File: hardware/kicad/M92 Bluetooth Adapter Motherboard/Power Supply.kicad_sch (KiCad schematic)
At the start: 35 parts, among them IC11 MCP1702T-5002E_CB, IC12 TPS22810DBVR, IC13 TPS22917DBVR, IC4 NJU7031D, IC4 TL7660IDR, J1 Conn_External_Power, J4 B2B-XH-A, J5 B2B-XH-A, J9 B6B-XH-A

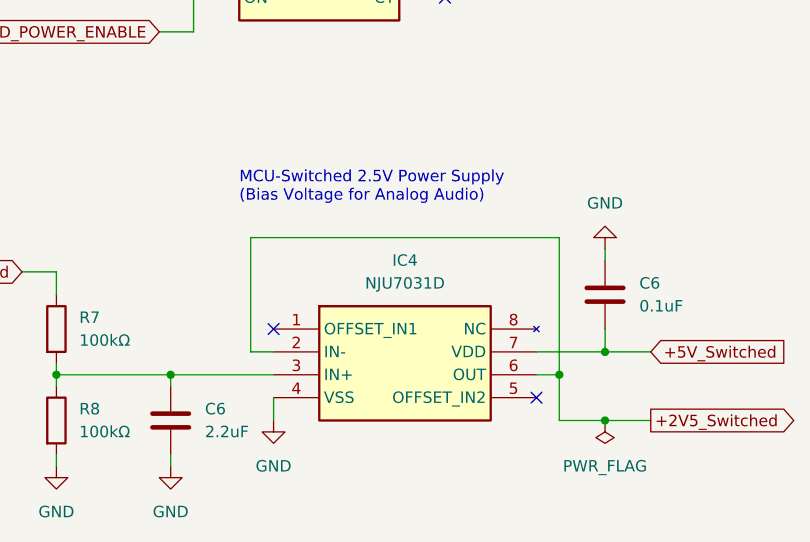
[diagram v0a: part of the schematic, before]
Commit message: Rework load switch enable circuitry/code
Rework load switch enable circuitry/code to fix brief power-on glitch when initially connecting battery power.
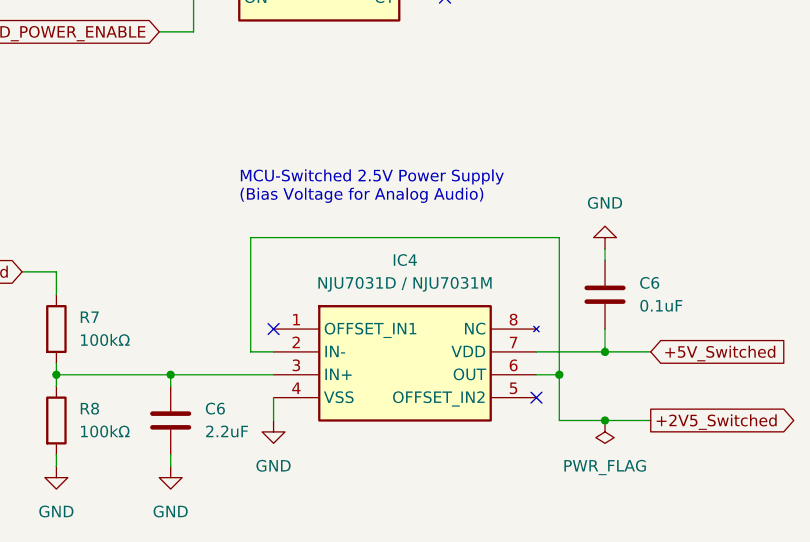
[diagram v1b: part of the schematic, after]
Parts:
- IC4: value NJU7031D -> NJU7031D / NJU7031M
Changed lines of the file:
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@@
       (effects (font (size 1.27 1.27)))
     )
-    (property "Value" "NJU7031D" (at 88.265 168.91 0)
+    (property "Value" "NJU7031D / NJU7031M" (at 88.265 168.91 0)
       (effects (font (size 1.27 1.27)))
     )

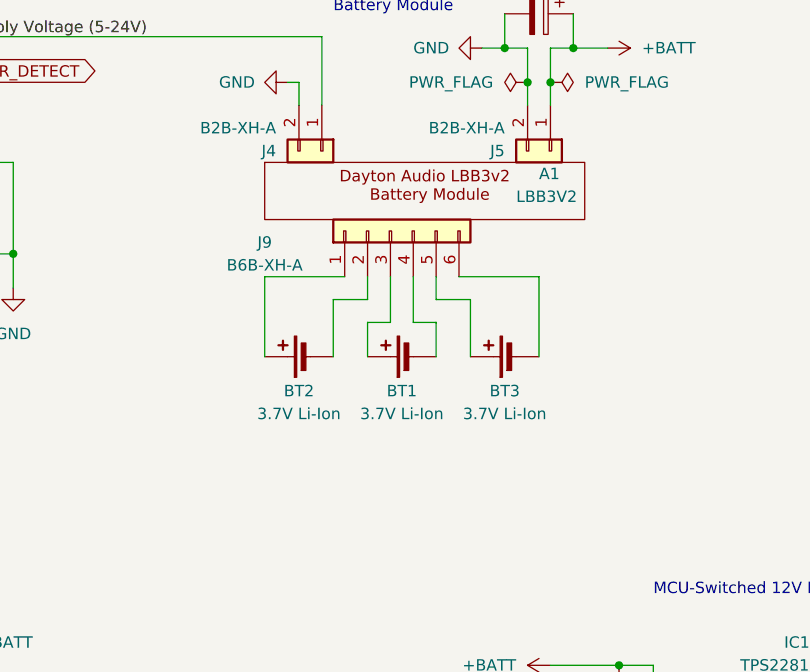
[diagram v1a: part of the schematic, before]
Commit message: Partial motherboard PCB updates for test fitting
This is a partial update to the motherboard PCB layout just so I can get some prototype boards manufactured and test fit with some updated/relocated components before committing to laying out the new custom battery/power management circuitry.

* Removed representation of Dayton Audio battery module PCB (will be replaced by custom battery circuitry in future).
* Relocated battery holders, and updated their footprints for sturdier part.
* Added pin headers for mounting the new programming port PCB.
* Adjusted positions of several mounting holes in attempt to match reality better (based on actual fitment of the PCB).
* Adjusted position of BT module connector slightly right in attempt to match reality better (based on actual fitment of the PCB).
* Adjusted footprint of mic jack to use oval PTH.
* Adjusted mic jack position further toward front edge of board to protrude more like original car phone mic jack.
* Added custom 3D models for BT module connector, RJ45 socket, and coax antenna port.
* Added coax antenna port and programming port to the PCB layout for spatial reference (not on schematic)
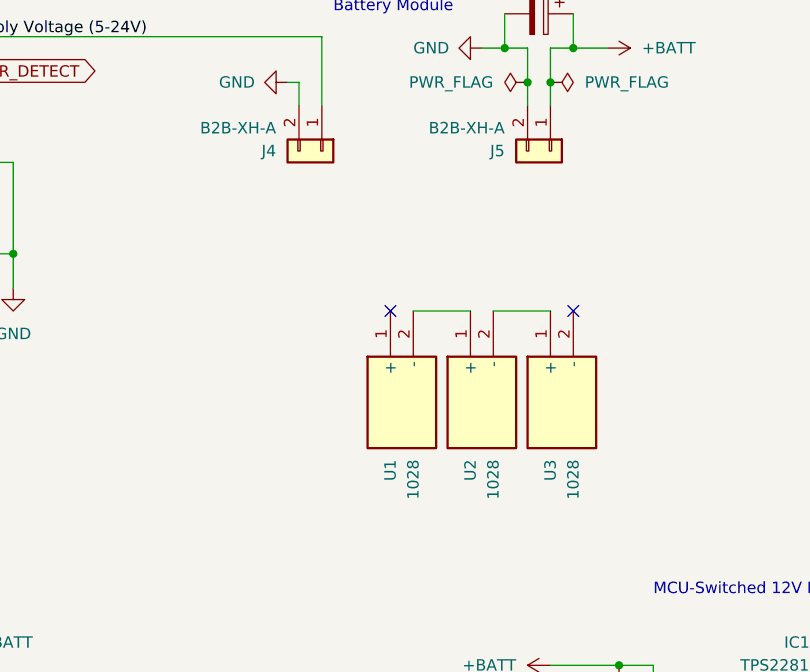
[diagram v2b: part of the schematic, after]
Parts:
- removed A1: LBB3V2, M92 Bluetooth Adapter Motherboard:LBB3v2 Battery Module, symbol M92 Bluetooth Adapter Motherboard:LBB3V2
- removed BT1, BT2, BT3: 3.7V Li-Ion, Battery:BatteryHolder_Keystone_2460_1xAA, symbol Device:Battery_Cell
- removed J9: B6B-XH-A, Connector_JST:JST_XH_B6B-XH-A_1x06_P2.50mm_Vertical, symbol Connector_Generic:Conn_01x06
- added U1, U2, U3: 1028, SamacSys_Parts:1028, symbol SamacSys_Parts:1028
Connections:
- new net: U1.2 (-), U2.1 (+)
- new net: U2.2 (-), U3.1 (+)
- no-connect marks 6 -> 8

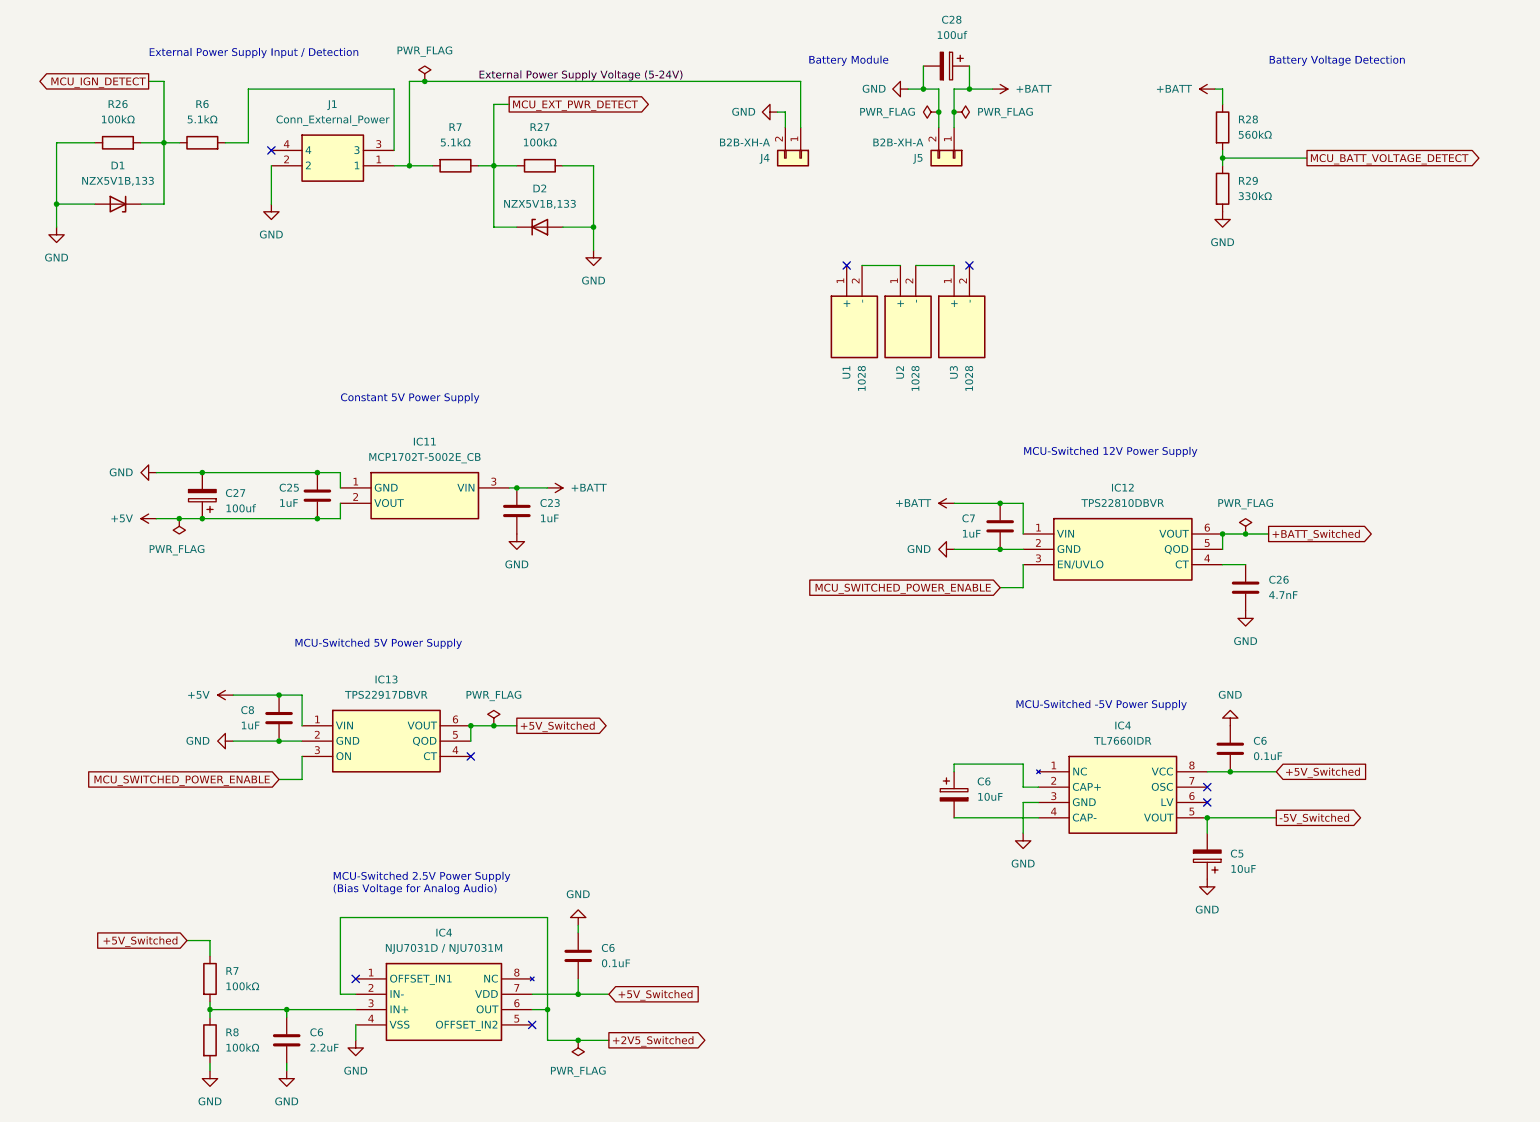
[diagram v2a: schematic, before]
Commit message: Add new battery module to motherboard schematic
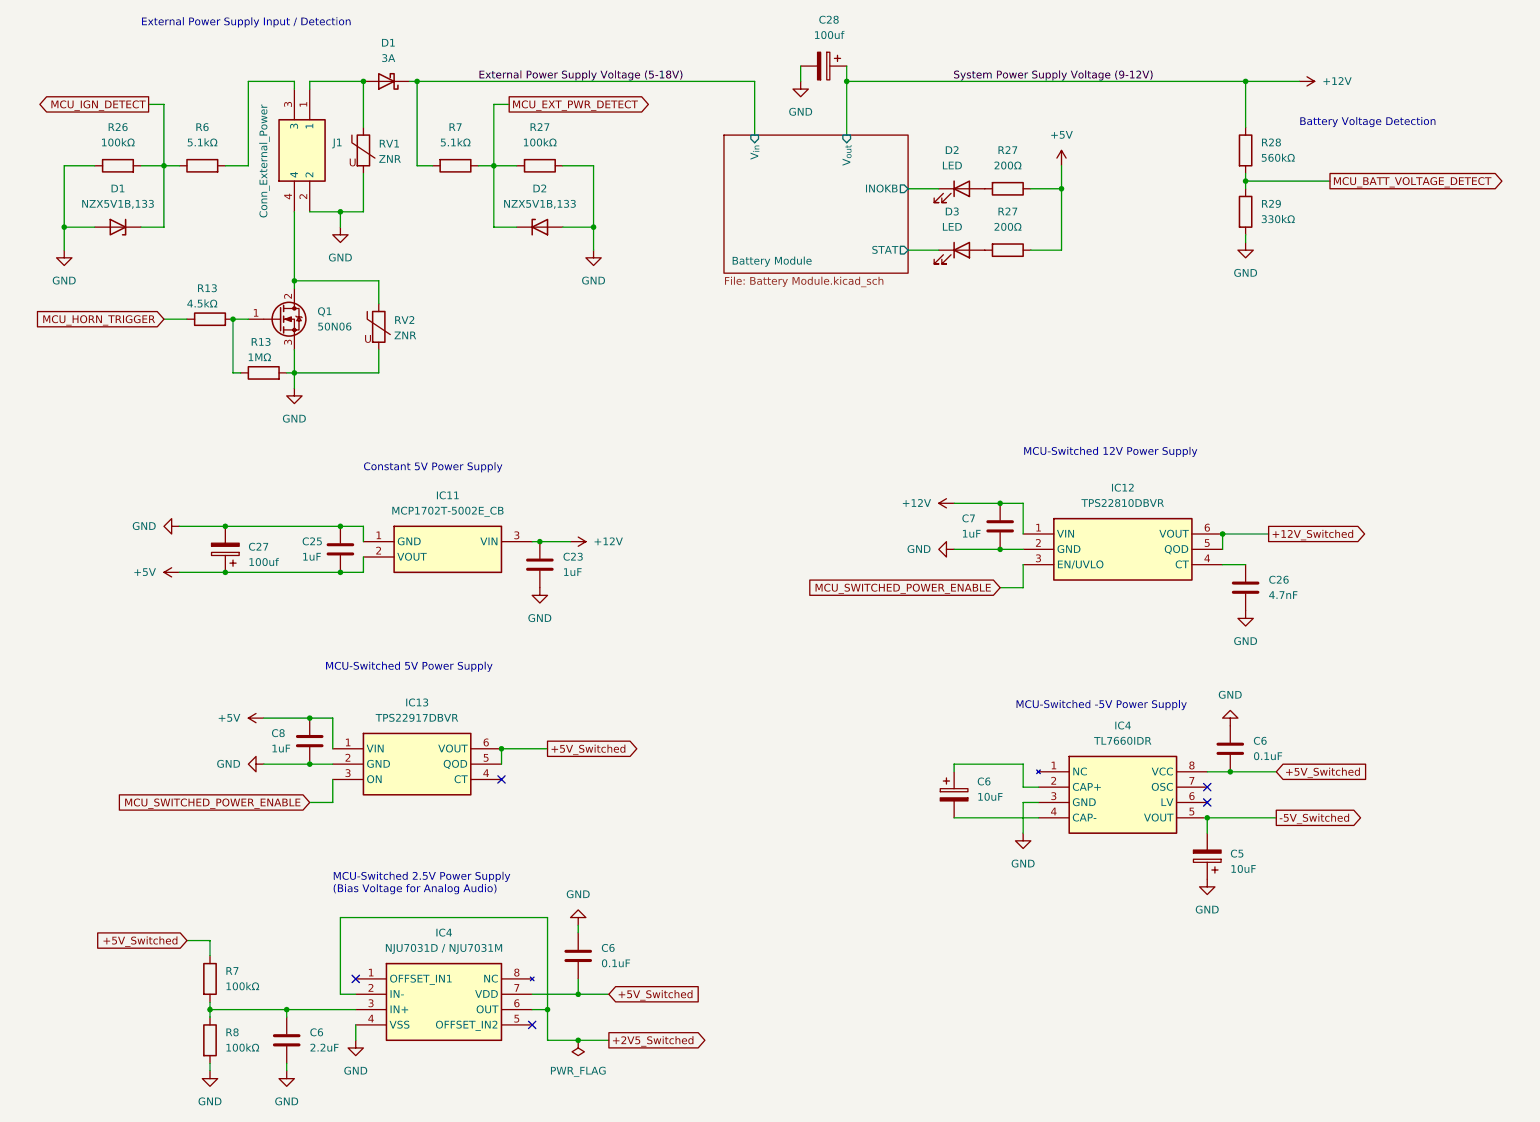
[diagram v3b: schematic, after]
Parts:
- removed J4, J5: B2B-XH-A, Connector_JST:JST_XH_B2B-XH-A_1x02_P2.50mm_Vertical, symbol Connector_Generic:Conn_01x02
- removed U1, U2, U3: 1028, SamacSys_Parts:1028, symbol SamacSys_Parts:1028
- added D1: 3A, Diode_THT:D_DO-201AD_P12.70mm_Horizontal, symbol Device:D_Schottky
- added D2, D3: LED, LED_SMD:LED_0805_2012Metric, symbol Device:LED
- added Q1: 50N06, Package_TO_SOT_SMD:TO-252-2, symbol Device:Q_NMOS_GDS
- added R13: 4.5kΩ, Resistor_SMD:R_0402_1005Metric, symbol Device:R
- added R13: 1MΩ, Resistor_SMD:R_0402_1005Metric, symbol Device:R
- added R27 (x2): 200Ω, Resistor_SMD:R_0402_1005Metric, symbol Device:R
- added RV1, RV2: ZNR, M92 Bluetooth Adapter Motherboard:ERZV10D270, symbol Device:Varistor
- IC11: Mouser Price/Stock https://www.mouser.com/ProductDetail/Microchip-Technology/M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 -> https://www.mouser.co.uk/ProductDetail/Microchip-Technology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
- IC12, IC13: Mouser Price/Stock https://www.mouser.com/ProductDetail/Texas-Instruments/TPS2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 -> https://www.mouser.co.uk/ProductDetail/Texas-Instruments/TP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
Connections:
- net +5V: now also R27.1, R27.1
- net GND: now also Q1.3 (S), R13.2, RV1.2, RV2.2
- net at J1.4: now also Q1.2 (D), RV2.1
- net +BATT renamed +12V
- net +BATT_Switched renamed +12V_Switched
- net External Power Supply Voltage (5-24V): no longer names the net of J1.1
- net External Power Supply Voltage (5-24V): now also D1.2 (A), RV1.1; no longer R7.2
- new net: D3.2 (A), R27.2
- new net: Q1.1 (G), R13.1, R13.2
- new net: D2.2 (A), R27.2
- new net Battery Module/INOKB: D2.1 (K)
- new net Battery Module/STAT: D3.1 (K)
- new net External Power Supply Voltage (5-18V): D1.1 (K), R7.2
- new net MCU_HORN_TRIGGER: R13.1
- no-connect marks 8 -> 5
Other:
- added sheet Battery Module (Battery Module.kicad_sch)
- note removed: "Battery Module"
- moved on the sheet: C23, C25, C27, C28, C8, D1, IC11, IC13, J1, R26, R28, R29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
